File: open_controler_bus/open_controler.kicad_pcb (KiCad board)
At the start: 2 copper layers, 120.1 x 61.9 mm, 4 parts, among them J1 02x200, J2 02x20, J3 02x20, J4 02x20

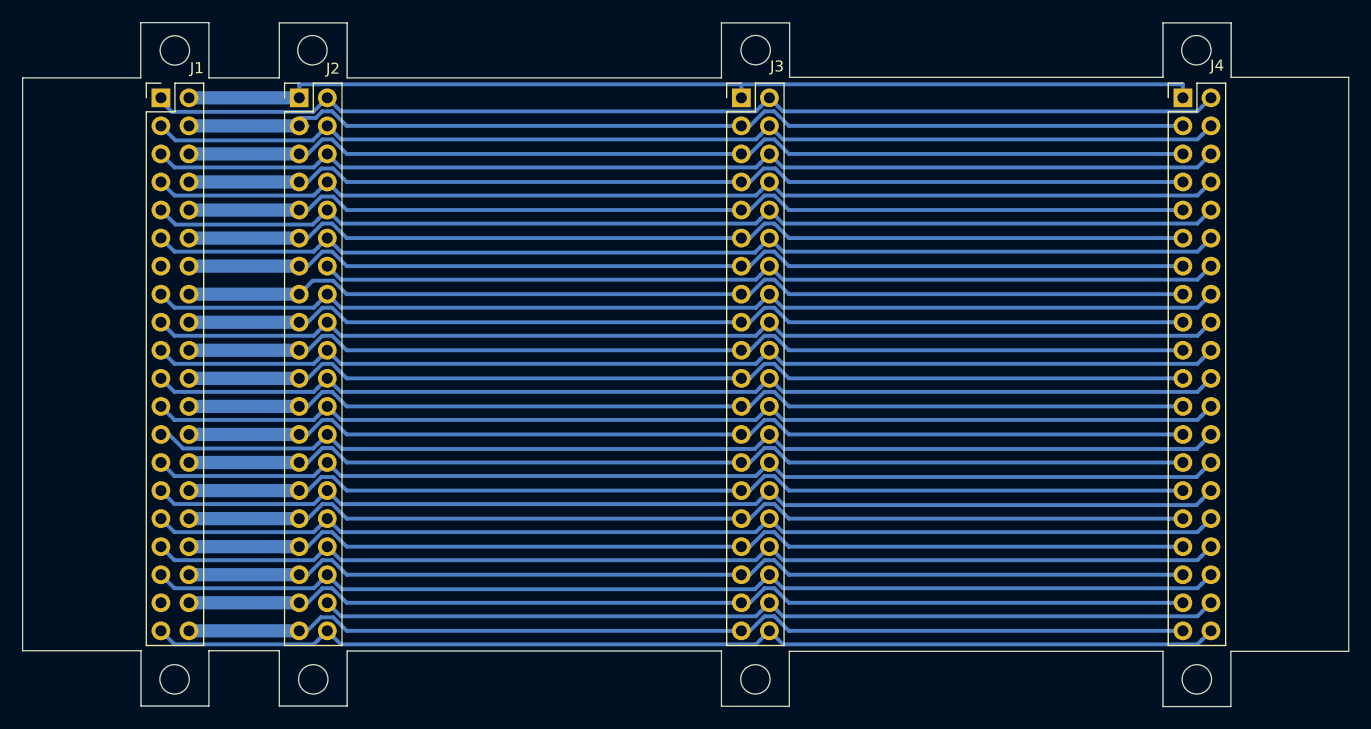
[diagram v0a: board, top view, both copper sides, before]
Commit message: 3d anadido a open controles bus
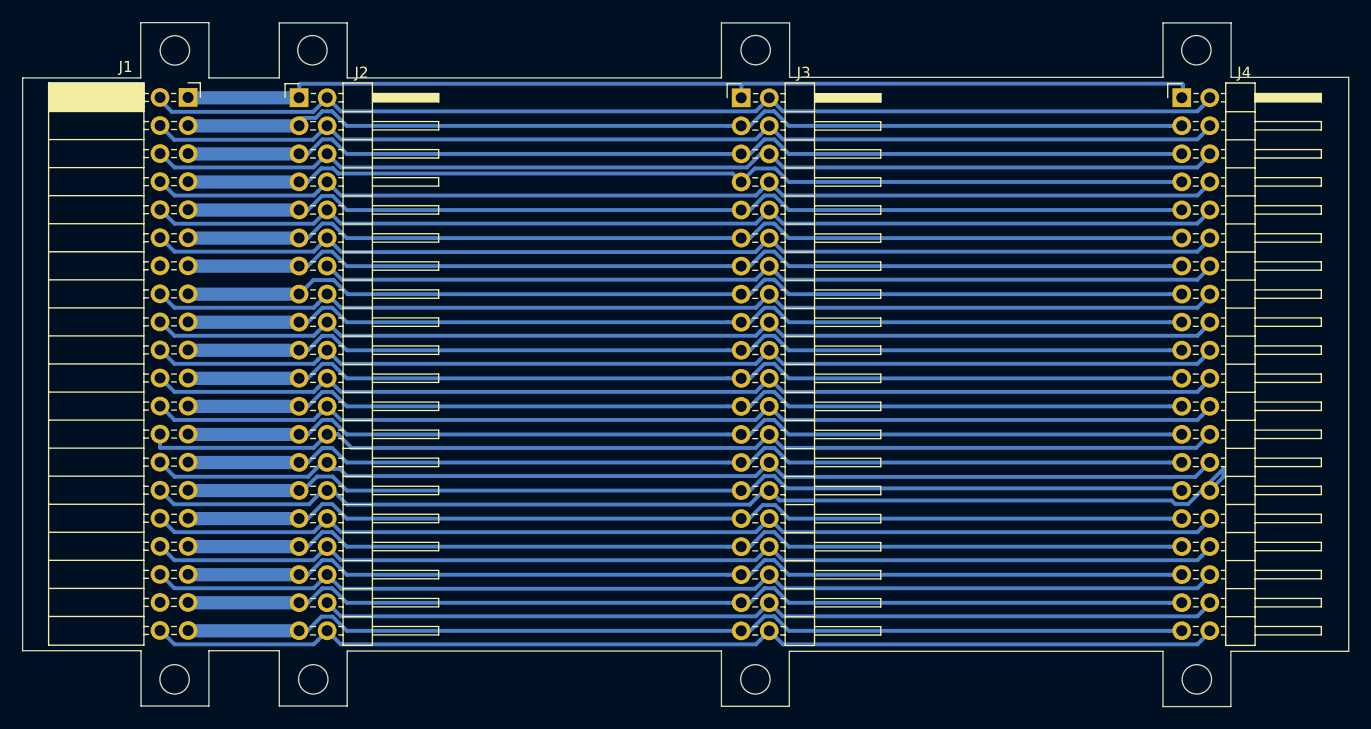
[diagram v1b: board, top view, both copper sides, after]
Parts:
- J1: value 02x200 -> Conn_02x20_Odd_Even; footprint Connector_PinHeader_2.54mm:PinHeader_2x20_P2.54mm_Vertical -> Connector_PinSocket_2.54mm:PinSocket_2x20_P2.54mm_Horizontal
- J2, J3, J4: value 02x20 -> Conn_02x20_Odd_Even; footprint Connector_PinHeader_2.54mm:PinHeader_2x20_P2.54mm_Vertical -> Connector_PinHeader_2.54mm:PinHeader_2x20_P2.54mm_Horizontal
- moved J1 2.46 mm to (84.2, 59.1)
- moved J4 0.11 mm to (174.2, 59.1)
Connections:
- J1 pad 1: 3v3_1 -> 5v_1
- J1 pad 10: GPIO_15 -> GND_2
- J1 pad 11: GPIO_17 -> GPIO_18
- J1 pad 12: GPIO_18 -> GPIO_17
- J1 pad 13: Net-(J1-Pad13) -> GND_3
- J1 pad 14: GND_3 -> Net-(J1-Pad14)
- J1 pad 15: GPIO_22 -> GPIO_23
- J1 pad 16: GPIO_23 -> GPIO_22
- J1 pad 17: 3v3_2 -> GPIO_24
- J1 pad 18: GPIO_24 -> 3v3_2
- J1 pad 19: GPIO_10 -> GND_4
- J1 pad 2: 5v_1 -> 3v3_1
- J1 pad 20: GND_4 -> GPIO_10
- J1 pad 21: GPIO_9 -> GPIO_25
- J1 pad 22: GPIO_25 -> GPIO_9
- J1 pad 23: GPIO_11 -> GPIO_8
- J1 pad 24: GPIO_8 -> GPIO_11
- J1 pad 25: GND_5 -> GPIO_7
- J1 pad 26: GPIO_7 -> GND_5
- J1 pad 27: GPIO_0 -> GPIO_1
- J1 pad 28: GPIO_1 -> GPIO_0
- J1 pad 29: GPIO_5 -> GND_6
- J1 pad 3: GPIO_2 -> 5v_2
- J1 pad 30: GND_6 -> GPIO_5
- J1 pad 31: GPIO_6 -> GPIO_12
- J1 pad 32: GPIO_12 -> GPIO_6
- J1 pad 33: GPIO_13 -> GND_7
- J1 pad 34: GND_7 -> GPIO_13
- J1 pad 35: GPIO_19 -> GPIO_16
- J1 pad 36: GPIO_16 -> GPIO_19
- J1 pad 37: Net-(J1-Pad37) -> GPIO_20
- J1 pad 38: GPIO_20 -> Net-(J1-Pad38)
- J1 pad 39: GND_8 -> GPIO_21
- J1 pad 4: 5v_2 -> GPIO_2
- J1 pad 40: GPIO_21 -> GND_8
- J1 pad 5: GPIO_3 -> GND_1
- J1 pad 6: GND_1 -> GPIO_3
- J1 pad 7: GPIO_4 -> GPIO_14
- J1 pad 8: GPIO_14 -> GPIO_4
- J1 pad 9: GND_2 -> GPIO_15
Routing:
- net GPIO_5: track 98.2 -> 102.7 mm
- net 5v_2: track 93.3 -> 92.5 mm
- net GND_5: track 98.3 -> 98.8 mm
